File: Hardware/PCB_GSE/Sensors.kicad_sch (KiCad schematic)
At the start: 18 parts, among them J7 Screw_Terminal_01x04, J8 Screw_Terminal_01x04, U11 MAX6612MXK, U9 INA125UA/2K5

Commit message: fix : done silkscreen and finition
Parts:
- renumbered C57 to C17, C58 to C27, C60 to C29, C59 to C32, C61 to C6, C62 to C7, D5 to D3, D4 to D5, J7 to J6, J8 to J7, R46 to R16, R49 to R19, R39 to R25, R37 to R29, R45 to R30, R44 to R4, U11 to U1, U9 to U4
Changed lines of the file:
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@@
 		(on_board yes)
 		(dnp no)
-		(property "Reference" "D4"
+		(property "Reference" "D5"
 			(at 69.596 66.04 90)
 			(effects
@@
 			(project "PCB_GSE"
 				(path "/a63f9ed4-21e4-42d0-8bfc-f96143f84d4d/03aa44f0-76dc-422b-9f36-66afc2e68b3b"
-					(reference "D4")
+					(reference "D5")
 					(unit 1)
 				)
@@
 		(dnp no)
 		(fields_autoplaced yes)
-		(property "Reference" "D5"
+		(property "Reference" "D3"
 			(at 124.46 137.1599 90)
 			(effects
@@
 			(project "PCB_GSE"
 				(path "/a63f9ed4-21e4-42d0-8bfc-f96143f84d4d/03aa44f0-76dc-422b-9f36-66afc2e68b3b"
-					(reference "D5")
+					(reference "D3")
 					(unit 1)
 				)
@@
 		(on_board yes)
 		(dnp no)
-		(property "Reference" "R49"
+		(property "Reference" "R19"
 			(at 137.668 134.874 90)
 			(effects
@@
 			(project "PCB_GSE"
 				(path "/a63f9ed4-21e4-42d0-8bfc-f96143f84d4d/03aa44f0-76dc-422b-9f36-66afc2e68b3b"
-					(reference "R49")
+					(reference "R19")
 					(unit 1)
 				)
@@
 		(on_board yes)
 		(dnp no)
-		(property "Reference" "R45"
+		(property "Reference" "R30"
 			(at 60.96 57.1499 0)
 			(effects
@@
 			(project "PCB_GSE"
 				(path "/a63f9ed4-21e4-42d0-8bfc-f96143f84d4d/03aa44f0-76dc-422b-9f36-66afc2e68b3b"
-					(reference "R45")
+					(reference "R30")
 					(unit 1)
 				)
@@
 		(dnp no)
 		(fields_autoplaced yes)
-		(property "Reference" "U9"
+		(property "Reference" "U4"
 			(at 77.47 113.03 0)
 			(effects
@@
 			(project "PCB_GSE"
 				(path "/a63f9ed4-21e4-42d0-8bfc-f96143f84d4d/03aa44f0-76dc-422b-9f36-66afc2e68b3b"
-					(reference "U9")
+					(reference "U4")
 					(unit 1)
 				)
@@
 		(on_board yes)
 		(dnp no)
-		(property "Reference" "C62"
+		(property "Reference" "C7"
 			(at 267.97 31.242 90)
 			(effects
@@
 			(project "PCB_GSE"
 				(path "/a63f9ed4-21e4-42d0-8bfc-f96143f84d4d/03aa44f0-76dc-422b-9f36-66afc2e68b3b"
-					(reference "C62")
+					(reference "C7")
 					(unit 1)
 				)
@@
 		(on_board yes)
 		(dnp no)
-		(property "Reference" "R37"
+		(property "Reference" "R29"
 			(at 50.292 56.388 0)
 			(effects
@@
 			)
 		)
+		(property "Purchase-URL" ""
+			(at 45.72 57.15 0)
+			(effects
+				(font
+					(size 1.27 1.27)
+				)
+				(hide yes)
+			)
+		)
+		(property "Sim.Device" ""
+			(at 45.72 57.15 0)
+			(effects
+				(font
+					(size 1.27 1.27)
+				)
+				(hide yes)
+			)
+		)
+		(property "Sim.Pins" ""
+			(at 45.72 57.15 0)
+			(effects
+				(font
+					(size 1.27 1.27)
+				)
+				(hide yes)
+			)
+		)
+		(property "Sim.Type" ""
+			(at 45.72 57.15 0)
+			(effects
+				(font
+					(size 1.27 1.27)
+				)
+				(hide yes)
+			)
+		)
 		(pin "1"
 		)
@@
 			(project "PCB_GSE"
 				(path "/a63f9ed4-21e4-42d0-8bfc-f96143f84d4d/03aa44f0-76dc-422b-9f36-66afc2e68b3b"
-					(reference "R37")
+					(reference "R29")
 					(unit 1)
 				)
@@
 		(on_board yes)
 		(dnp no)
-		(property "Reference" "R39"
+		(property "Reference" "R25"
 			(at 59.69 49.022 90)
 			(effects
@@
 			(project "PCB_GSE"
 				(path "/a63f9ed4-21e4-42d0-8bfc-f96143f84d4d/03aa44f0-76dc-422b-9f36-66afc2e68b3b"
-					(reference "R39")
+					(reference "R25")
 					(unit 1)
 				)
@@
 		(on_board yes)
 		(dnp no)
-		(property "Reference" "C61"
+		(property "Reference" "C6"
 			(at 258.826 42.164 0)
 			(effects
@@
 			(project "PCB_GSE"
 				(path "/a63f9ed4-21e4-42d0-8bfc-f96143f84d4d/03aa44f0-76dc-422b-9f36-66afc2e68b3b"
-					(reference "C61")
+					(reference "C6")
 					(unit 1)
 				)
@@
 		(dnp no)
 		(fields_autoplaced yes)
-		(property "Reference" "U11"
+		(property "Reference" "U1"
 			(at 240.03 26.67 0)
 			(effects
@@
 			(project "PCB_GSE"
 				(path "/a63f9ed4-21e4-42d0-8bfc-f96143f84d4d/03aa44f0-76dc-422b-9f36-66afc2e68b3b"
-					(reference "U11")
+					(reference "U1")
 					(unit 1)
 				)
@@
 		(on_board yes)
 		(dnp no)
-		(property "Reference" "C60"
+		(property "Reference" "C29"
 			(at 137.922 139.954 0)
 			(effects
@@
 			(project "PCB_GSE"
 				(path "/a63f9ed4-21e4-42d0-8bfc-f96143f84d4d/03aa44f0-76dc-422b-9f36-66afc2e68b3b"
-					(reference "C60")
+					(reference "C29")
 					(unit 1)
 				)
@@
 		(on_board yes)
 		(dnp no)
-		(property "Reference" "R46"
+		(property "Reference" "R16"
 			(at 79.756 147.828 90)
 			(effects
@@
 			(project "PCB_GSE"
 				(path "/a63f9ed4-21e4-42d0-8bfc-f96143f84d4d/03aa44f0-76dc-422b-9f36-66afc2e68b3b"
-					(reference "R46")
+					(reference "R16")
 					(unit 1)
 				)
@@
 		(on_board yes)
 		(dnp no)
-		(property "Reference" "J7"
+		(property "Reference" "J6"
 			(at 129.794 109.22 0)
 			(effects
@@
 			(project "PCB_GSE"
 				(path "/a63f9ed4-21e4-42d0-8bfc-f96143f84d4d/03aa44f0-76dc-422b-9f36-66afc2e68b3b"
-					(reference "J7")
+					(reference "J6")
 					(unit 1)
 				)
@@
 		(on_board yes)
 		(dnp no)
-		(property "Reference" "C58"
+		(property "Reference" "C27"
 			(at 40.132 36.068 90)
 			(effects
@@
 			(project "PCB_GSE"
 				(path "/a63f9ed4-21e4-42d0-8bfc-f96143f84d4d/03aa44f0-76dc-422b-9f36-66afc2e68b3b"
-					(reference "C58")
+					(reference "C27")
 					(unit 1)
 				)
@@
 		(on_board yes)
 		(dnp no)
-		(property "Reference" "R44"
+		(property "Reference" "R4"
 			(at 38.862 142.748 0)
 			(effects
@@
 			(project "PCB_GSE"
 				(path "/a63f9ed4-21e4-42d0-8bfc-f96143f84d4d/03aa44f0-76dc-422b-9f36-66afc2e68b3b"
-					(reference "R44")
+					(reference "R4")
 					(unit 1)
 				)
@@
 		(on_board yes)
 		(dnp no)
-		(property "Reference" "C59"
+		(property "Reference" "C32"
 			(at 82.296 54.864 0)
 			(effects
@@
 			(project "PCB_GSE"
 				(path "/a63f9ed4-21e4-42d0-8bfc-f96143f84d4d/03aa44f0-76dc-422b-9f36-66afc2e68b3b"
-					(reference "C59")
+					(reference "C32")
 					(unit 1)
 				)
@@
 		(on_board yes)
 		(dnp no)
-		(property "Reference" "J8"
+		(property "Reference" "J7"
 			(at 37.846 59.182 0)
 			(effects
@@
 			(project "PCB_GSE"
 				(path "/a63f9ed4-21e4-42d0-8bfc-f96143f84d4d/03aa44f0-76dc-422b-9f36-66afc2e68b3b"
-					(reference "J8")
+					(reference "J7")
 					(unit 1)
 				)
@@
 		(on_board yes)
 		(dnp no)
-		(property "Reference" "C57"
+		(property "Reference" "C17"
 			(at 34.798 113.538 90)
 			(effects
@@
 			(project "PCB_GSE"
 				(path "/a63f9ed4-21e4-42d0-8bfc-f96143f84d4d/03aa44f0-76dc-422b-9f36-66afc2e68b3b"
-					(reference "C57")
+					(reference "C17")
 					(unit 1)
 				)

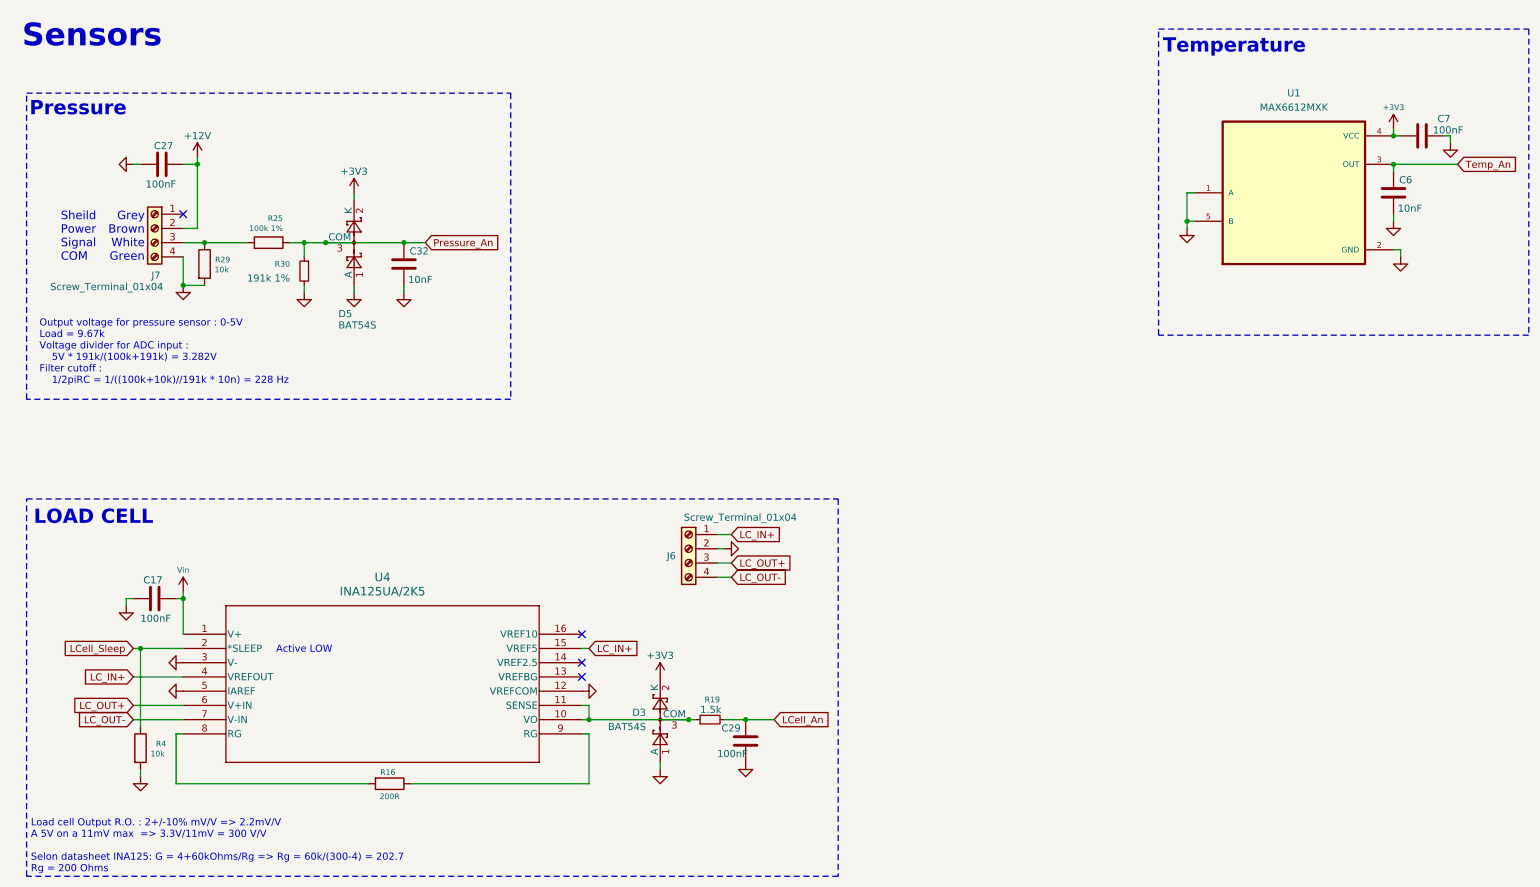
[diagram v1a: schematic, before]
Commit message: fix(gse): Vin servo
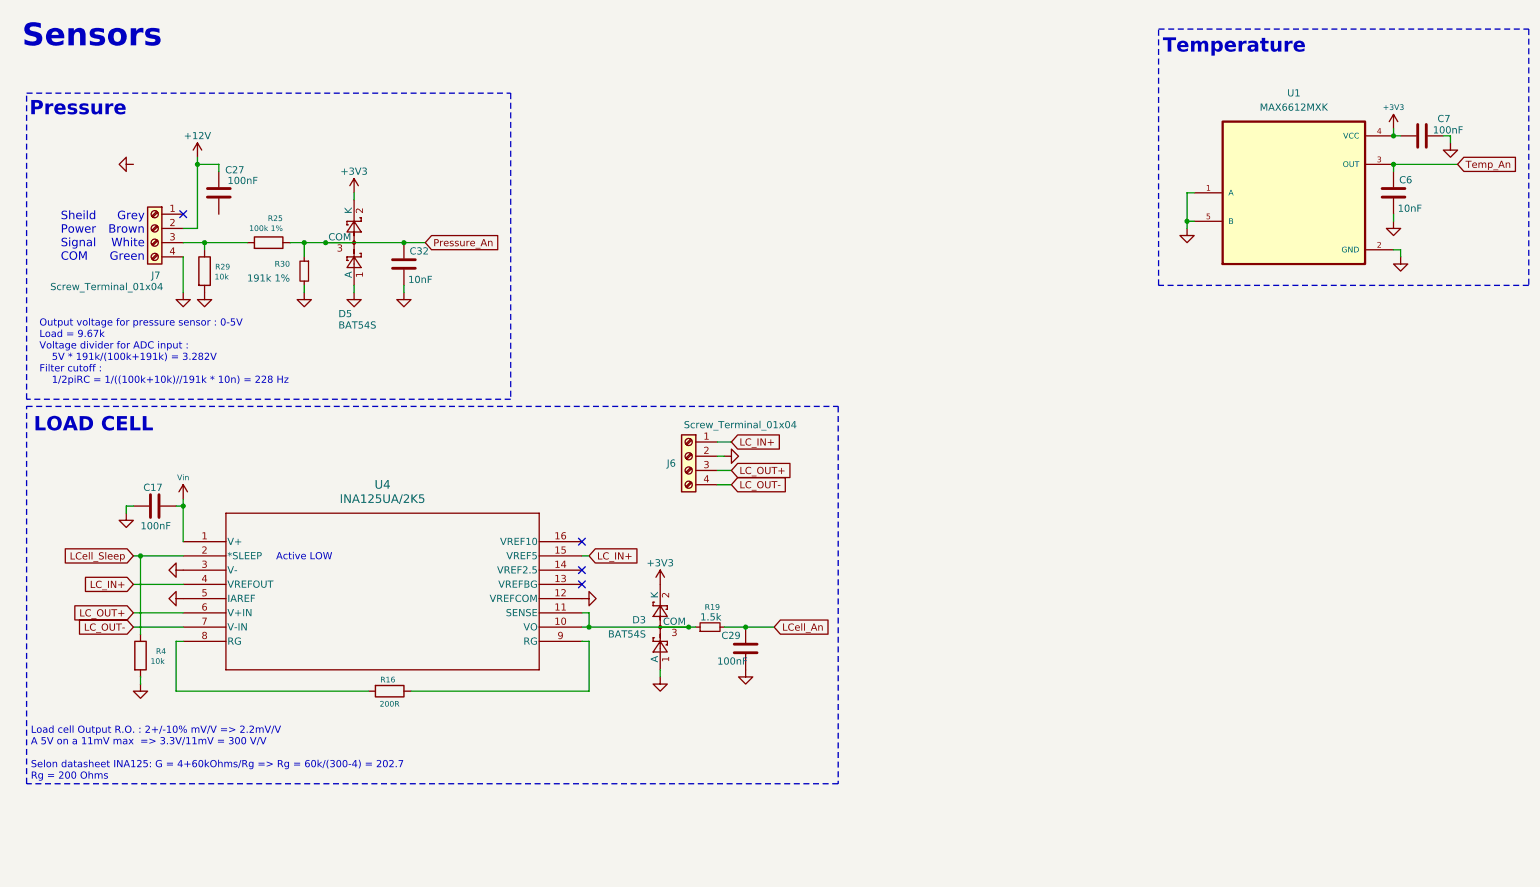
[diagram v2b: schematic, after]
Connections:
- net +12V: now also C27.1; no longer C27.2
- net GND: no longer C27.1
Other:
- moved on the sheet: C17, C27, C29, D3, J6, R16, R19, R29, R4, U4

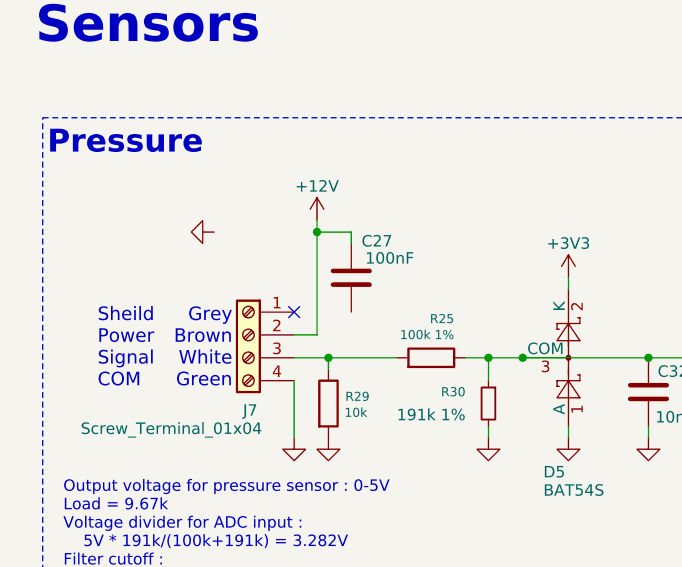
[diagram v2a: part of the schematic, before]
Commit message: fix(moteur + gse): gnd not connected for pressure sensor + seperate alim pressure sensor for motor pcb
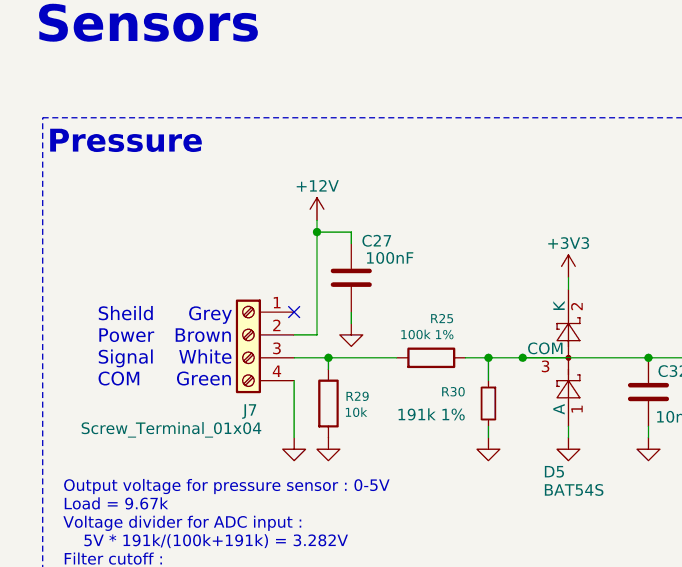
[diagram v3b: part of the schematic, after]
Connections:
- net GND: now also C27.2
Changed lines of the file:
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@@
+	(wire
+		(pts
+			(xy 48.26 48.26) (xy 48.26 49.53)
+		)
+		(stroke
+			(width 0)
+			(type default)
+		)
+	)
 	(wire
 		(pts
@@
 	(symbol
 		(lib_id "power:GND")
-		(at 33.02 39.37 270)
+		(at 48.26 49.53 0)
 		(unit 1)
 		(exclude_from_sim no)
@@
 		(fields_autoplaced yes)
 		(property "Reference" "#PWR011"
-			(at 26.67 39.37 0)
+			(at 48.26 55.88 0)
 			(effects
 				(font
@@
 		)
 		(property "Value" "GND"
-			(at 27.94 39.37 0)
+			(at 48.26 54.61 0)
 			(effects
 				(font
@@
 		)
 		(property "Footprint" ""
-			(at 33.02 39.37 0)
+			(at 48.26 49.53 0)
 			(effects
 				(font
@@
 		)
 		(property "Datasheet" ""
-			(at 33.02 39.37 0)
+			(at 48.26 49.53 0)
 			(effects
 				(font
@@
 		)
 		(property "Description" ""
-			(at 33.02 39.37 0)
-			(effects
-				(font
+			(at 48.26 49.53 0)
+			(effects
+				(font

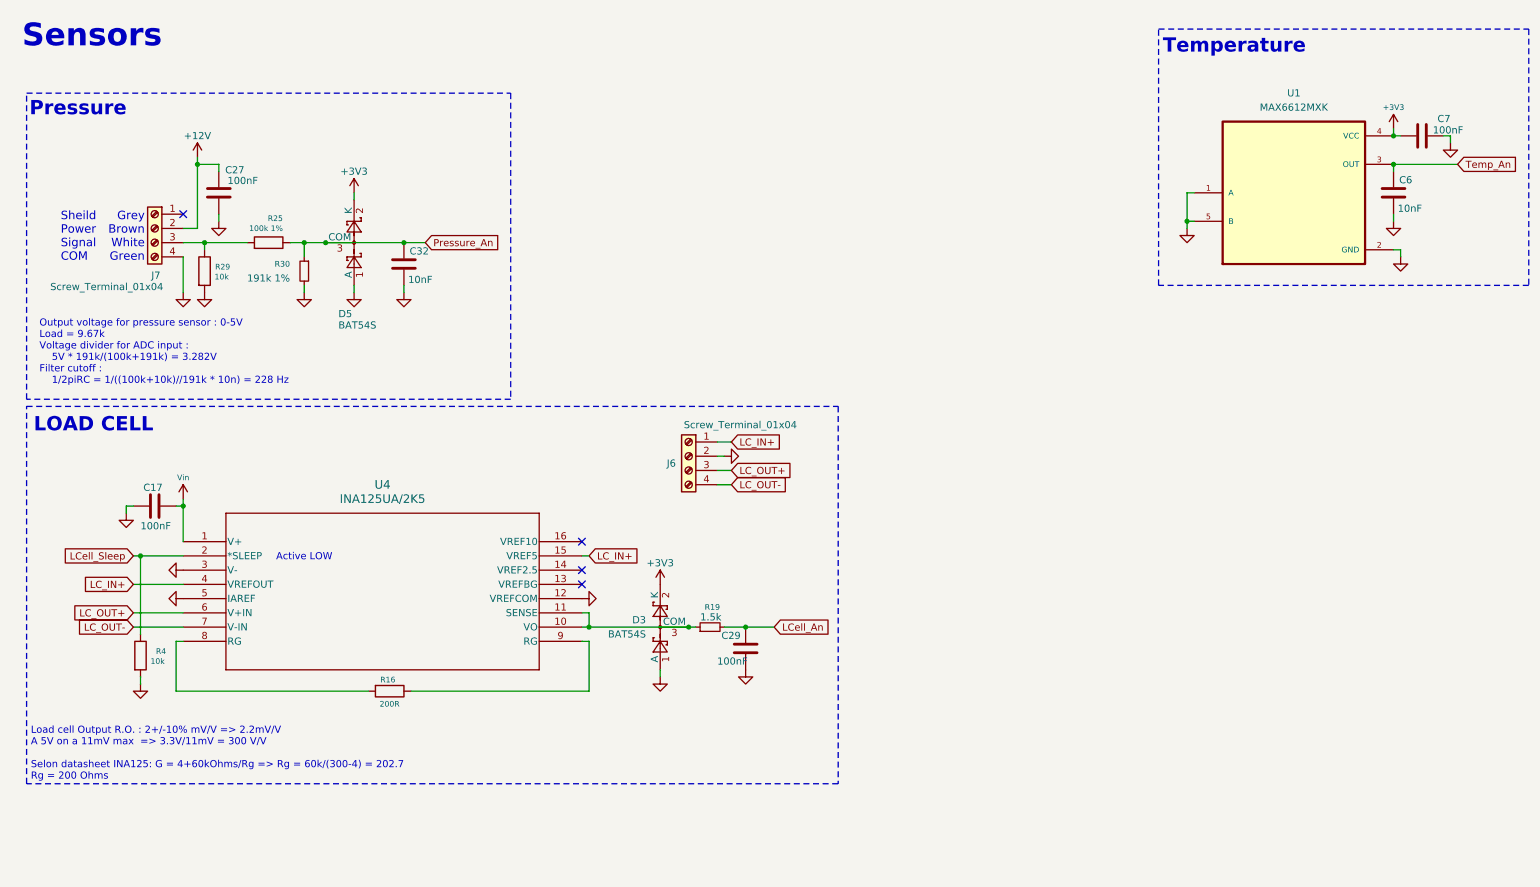
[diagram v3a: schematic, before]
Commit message: fix: silkscreen green<->black + fix silkscreen + connect shield to gnd  in pressure sensor + fix/add doc
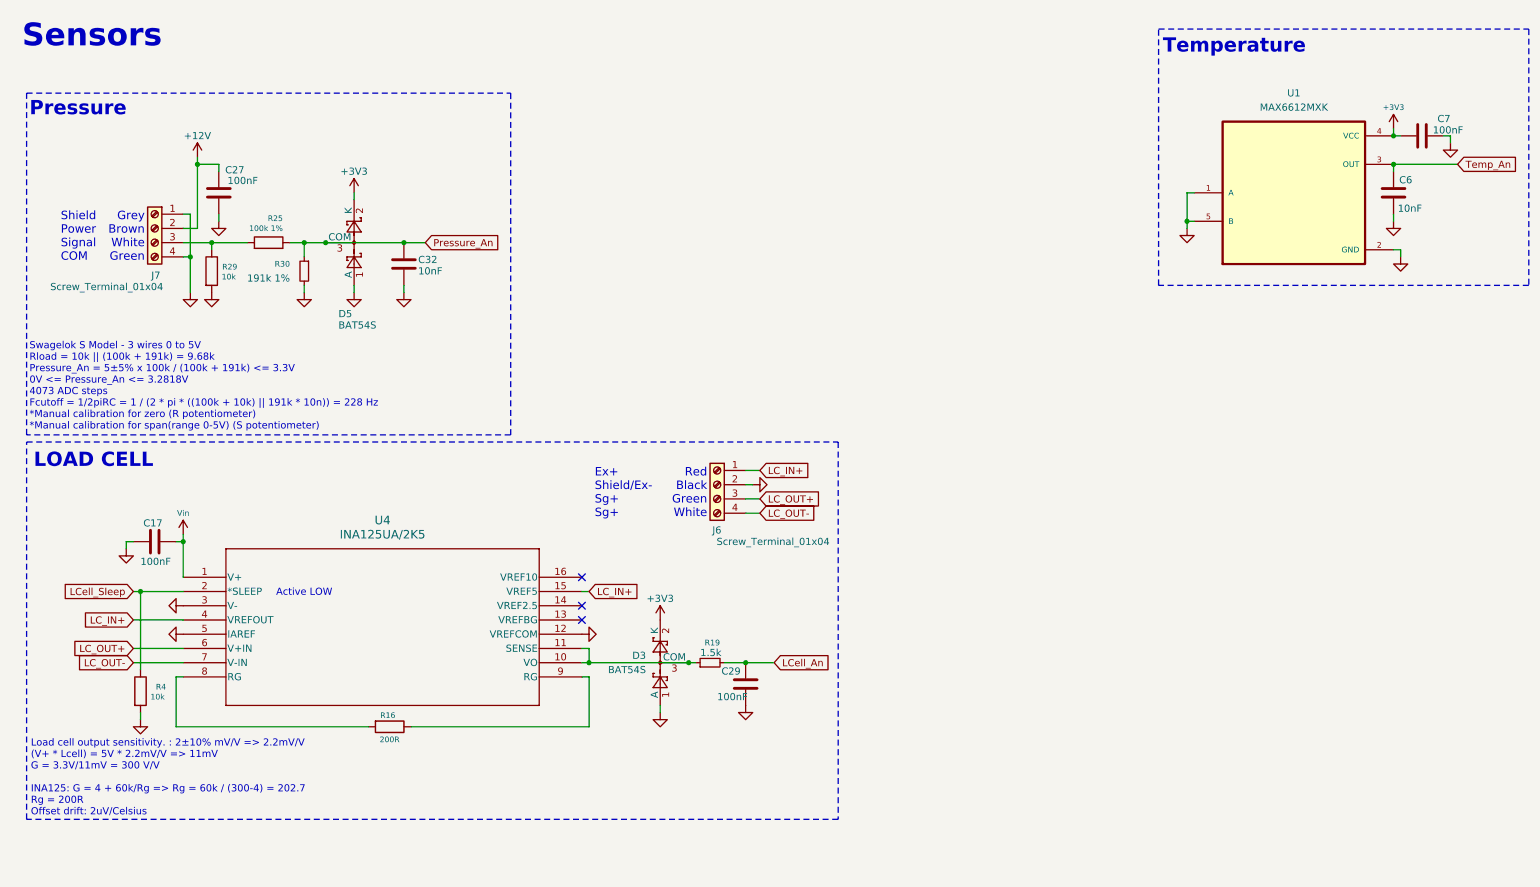
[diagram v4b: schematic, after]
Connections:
- net GND: now also J7.1 (Pin_1)
- no-connect marks 4 -> 3
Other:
- note added: "Ex+ Shield/Ex- Sg+ Sg+"
- note added: "Load cell output sensitivity. : 2±10% mV/V => 2.2mV/V (V+ * Lcell) = 5V * 2.2mV/V => 11mV G = 3.3V/11mV = 300 V/V INA125: G = 4 + 60k/Rg => Rg = 60k / (300-4) = 202.7 Rg = 200R Offset drift: 2uV/Celsius"
- note added: "Red Black Green White"
- note added: "Shield Power Signal COM"
- note added: "Swagelok S Model - 3 wires 0 to 5V Rload = 10k || (100k + 191k) = 9.68k Pressure_An = 5±5% x 100k / (100k + 191k) <= 3.3V 0V <= Pressure_An <= 3.2818V 4073 ADC steps Fcutoff = 1/2piRC = 1 / (2 * pi * ((100k + 10k) || 191k * 10n)) = 228 Hz *Manual calibration for zero (R potentiometer) *Manual calibration for span(range 0-5V) (S potentiometer)"
- note removed: "Load cell Output R.O. : 2+/-10% mV/V => 2.2mV/V A 5V on a 11mV max => 3.3V/11mV = 300 V/V Selon datasheet INA125: G = 4+60kOhms/Rg => Rg = 60k/(300-4) = 202.7 Rg = 200 Ohms"
- note removed: "Output voltage for pressure sensor : 0-5V Load = 9.67k Voltage divider for ADC input : 5V * 191k/(100k+191k) = 3.282V Filter cutoff : 1/2piRC = 1/((100k+10k)//191k * 10n) = 228 Hz"
- note removed: "Sheild Power Signal COM"
- moved on the sheet: C17, C29, D3, J6, R16, R19, R29, R4, U4
